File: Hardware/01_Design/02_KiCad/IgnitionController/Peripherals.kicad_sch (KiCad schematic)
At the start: 0 parts

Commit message: Peripherals Update
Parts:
- added C37, C38: 2.2uF, Capacitor_SMD:C_0805_2012Metric_Pad1.18x1.45mm_HandSolder, symbol Device:C
- added C39, C41: 1u, symbol Device:C_Small
- added C40, C42: 0.1u, symbol Device:C_Small
- added D19, D20, D21, D22: RED, symbol Device:LED
- added Q7: SS8050, Package_TO_SOT_SMD:TSOT-23_HandSoldering, symbol Transistor_BJT:SS8050
- added R40, R41: 10K, symbol Device:R_Small
- added R45: 43k, Resistor_SMD:R_0805_2012Metric_Pad1.20x1.40mm_HandSolder, symbol Device:R
- added R46, R47, R52, R53: 10K, Resistor_SMD:R_0805_2012Metric_Pad1.20x1.40mm_HandSolder, symbol Device:R
- added R48, R49: 360R, Resistor_SMD:R_0805_2012Metric_Pad1.20x1.40mm_HandSolder, symbol Device:R
- added R50, R51, R60, R65: 2K, symbol Device:R_Small
- added R59, R62, R63, R64: 100R, Resistor_SMD:R_0805_2012Metric_Pad1.20x1.40mm_HandSolder, symbol Device:R
- added U14: AT24CS01-SSHM, Package_SO:SOIC-8_3.9x4.9mm_P1.27mm, symbol Memory_EEPROM:AT24CS01-SSHM
- added U15: MCP2557FD-xSN, Package_SO:SOIC-8_3.9x4.9mm_P1.27mm, symbol Interface_CAN_LIN:MCP2557FD-xSN
- added U19, U20: IXDN602, symbol Library_sym.pretty:IXDN602SIA
- added U23, U24: 4N35, Package_DIP:DIP-6_W7.62mm, symbol Isolator:4N35
- added U25: TXS0104EPW, Package_SO:TSSOP-14_4.4x5mm_P0.65mm, symbol Logic_LevelTranslator:TXS0104EPW
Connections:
- new net: U14.6 (SCL), U25.10 (B4)
- new net: U14.5 (SDA), U25.11 (B3)
- new net: U15.4 (RXD), U25.12 (B2)
- new net: U15.1 (TXD), U25.13 (B1)
- new net: Q7.2 (E), R46.1, U25.8 (OE)
- new net: C38.1, R49.2, U24.1
- new net: R64.2, U20.4 (INB)
- new net: R47.1, U15.8 (S)
- new net: D20.2 (A), R60.2
- new net: R41.2, U24.6
- new net: R62.2, U19.4 (INB)
- new net: Q7.1 (B), R45.1
- new net: R59.2, U19.2 (INA)
- new net: R63.2, U20.2 (INA)
- new net: D19.2 (A), R50.2
- new net: D21.2 (A), R65.2
- new net: D22.2 (A), R51.2
- new net: C37.1, R48.2, U23.1
- new net: R40.2, U23.6
- new net CAN_RXD: U25.3 (A2)
- new net CAN_TXD: U25.2 (A1)
- new net Cylinder1Out_Pin: R59.1
- new net Cylinder2Out_Pin: R62.1
- new net Cylinder3Out_Pin: R63.1
- new net Cylinder4Out_Pin: R64.1
- new net GND: C37.2, C38.2, C39.2, C40.2, C41.2, C42.2, D19.1 (K), D20.1 (K), D21.1 (K), D22.1 (K), R40.1, R41.1, R46.2, R47.2, R52.2, R53.2, U14.1 (A0), U14.2 (A1), U14.3 (A2), U14.4 (GND), U14.7 (WP), U15.2 (VSS), U19.3 (GND), U20.3 (GND), U23.2, U24.2, U25.7 (GND)
- new net I2C_SCL: U25.5 (A4)
- new net I2C_SDA: U25.4 (A3)
- new net IGN_COIL_DRV_1: R50.1, U19.7 (OUTA)
- new net IGN_COIL_DRV_2: R60.1, U19.5 (OUTB)
- new net IGN_COIL_DRV_3: R51.1, U20.7 (OUTA)
- new net IGN_COIL_DRV_4: R65.1, U20.5 (OUTB)
- new net KL30_OUT: C39.1, C40.1, C41.1, C42.1, U19.6 (VCC), U20.6 (VCC)
- new net OE_PIN2: R45.2
- new net SENSOR_1_SIGNAL: R48.1
- new net SENSOR_2_SIGNAL: R49.1
- new net Signal1_Pin: R52.1, U23.4
- new net Signal2_Pin: R53.1, U24.4
- new net VMCU_OUT: Q7.3 (C), U23.5, U24.5, U25.1 (V_{CCA})
- new net VSEN_OUT: U14.8 (VCC), U15.3 (VDD), U25.14 (V_{CCB})
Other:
- note added: "Crank Input Optocouplers"
- note added: "Ignition Output Driver"

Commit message: Updates to HW Layout
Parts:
- added C43, C48, C49: 1u, Capacitor_SMD:C_0805_2012Metric_Pad1.18x1.45mm_HandSolder, symbol Device:C_Small
- added C44, C50, C51: 0.1u, Capacitor_SMD:C_0805_2012Metric_Pad1.18x1.45mm_HandSolder, symbol Device:C_Small
- added C45, C46: 100n, Capacitor_SMD:C_0805_2012Metric_Pad1.18x1.45mm_HandSolder, symbol Device:C
- added C47: 0.1u, Capacitor_SMD:C_0805_2012Metric_Pad1.18x1.45mm_HandSolder, symbol Device:C
- added D27, D28, D29, D30: RED, LED_SMD:LED_1206_3216Metric_Pad1.42x1.75mm_HandSolder, symbol Device:LED
- added R58: 120R, Resistor_SMD:R_0805_2012Metric_Pad1.20x1.40mm_HandSolder, symbol Device:R
- added R70, R74: 7K, Resistor_SMD:R_0805_2012Metric_Pad1.20x1.40mm_HandSolder, symbol Device:R
- added R71, R75, R76: 10K, Resistor_SMD:R_0805_2012Metric_Pad1.20x1.40mm_HandSolder, symbol Device:R
- added R72, R73: 8.2K, Resistor_SMD:R_0805_2012Metric_Pad1.20x1.40mm_HandSolder, symbol Device:R
- added R77, R78, R79, R80: 100R, Resistor_SMD:R_0805_2012Metric_Pad1.20x1.40mm_HandSolder, symbol Device:R
- added R81, R82, R83, R84: 2K, Resistor_SMD:R_0805_2012Metric_Pad1.20x1.40mm_HandSolder, symbol Device:R_Small
- added U13: TLV2372, Package_SO:SOIC-8_5.3x6.2mm_P1.27mm, symbol Amplifier_Operational:TLV2372
- added U16: MAX232, Package_SO:SOIC-16_3.9x9.9mm_P1.27mm, symbol Interface_UART:MAX232
- added U21, U22: IXDN602, Package_SO:SO-8_3.9x4.9mm_P1.27mm, symbol Library_sym.pretty:IXDN602SIA
- C39, C40, C41, C42: footprint (none) -> Capacitor_SMD:C_0805_2012Metric_Pad1.18x1.45mm_HandSolder
- D19, D20, D21, D22: footprint (none) -> LED_SMD:LED_1206_3216Metric_Pad1.42x1.75mm_HandSolder
- R40, R41, R50, R51, R60, R65: footprint (none) -> Resistor_SMD:R_0805_2012Metric_Pad1.20x1.40mm_HandSolder
- U19, U20: footprint (none) -> Package_SO:SO-8_3.9x4.9mm_P1.27mm
- U23, U24: footprint Package_DIP:DIP-6_W7.62mm -> 4N35S:4N35S
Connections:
- net GND: now also C43.2, C44.2, C45.2, C46.2, C47.2, C48.2, C49.2, C50.2, C51.2, D27.1 (K), D28.1 (K), D29.1 (K), D30.1 (K), R71.2, R75.2, U13.4 (V-), U21.3 (GND), U22.3 (GND)
- net KL30_OUT: now also C48.1, C49.1, C50.1, C51.1, U21.6 (VCC), U22.6 (VCC)
- net VMCU_OUT: now also R76.1
- net VSEN_OUT: now also C43.1, C44.1
- net CAN-L: now reaches U15.6 (CANL)
- net CAN-L: now also R58.1
- net CAN-H: now reaches U15.7 (CANH)
- net CAN-H: now also R58.2
- new net: R74.2, R75.1, U13.5 (+)
- new net: R73.2, U13.6 (-), U13.7
- new net: R78.2, U21.4 (INB)
- new net: R72.2, U13.1, U13.2 (-)
- new net: R70.2, R71.1, U13.3 (+)
- new net: R77.2, U21.2 (INA)
- new net: D29.2 (A), R83.2
- new net: R79.2, U22.2 (INA)
- new net: R80.2, U22.4 (INB)
- new net: D27.2 (A), R81.2
- new net: D28.2 (A), R82.2
- new net: D30.2 (A), R84.2
- new net COOLANT_TEMP_ADC_SIGNAL: C47.1, R76.2
- new net Cylinder1FuelOut_Pin: R77.1
- new net Cylinder2FuelOut_Pin: R78.1
- new net Cylinder3FuelOut_Pin: R79.1
- new net Cylinder4FuelOut_Pin: R80.1
- new net FUEL_INJ_DRV_1: R83.1, U21.7 (OUTA)
- new net FUEL_INJ_DRV_2: R81.1, U21.5 (OUTB)
- new net FUEL_INJ_DRV_3: R84.1, U22.7 (OUTA)
- new net FUEL_INJ_DRV_4: R82.1, U22.5 (OUTB)
- new net MAP_SENSOR_ADC_SIGNAL: C45.1, R72.1
- new net MAP_SENSOR_SIGNAL: R70.1
- new net TPS_ADC_SIGNAL: C46.1, R73.1
- new net TPS_SIGNAL: R74.1
- new net VPMIC: U13.8 (V+)
- no-connect marks 0 -> 8
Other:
- note added: "Engine Sensors"
- note added: "Fuel Injector Driver"
- moved on the sheet: C37, C38, C39, C40, C41, C42, D19, D20, D21, D22, Q7, R40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

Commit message: Initial routing of Power supply
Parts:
- C37, C38, C39, C40, C41, C42, C43, C44, C45, C46, C47, C48, C49, C50, C51: footprint Capacitor_SMD:C_0805_2012Metric_Pad1.18x1.45mm_HandSolder -> Capacitor_SMD:C_0603_1608Metric_Pad1.08x0.95mm_HandSolder
- R40, R41, R45, R46, R47, R48, R49, R50, R51, R52, R53, R58, R59, R60, R62, R63, R64, R65, R70, R71, R72, R73, R74, R75, R76, R77, R78, R79, R80, R81, R82, R83, R84: footprint Resistor_SMD:R_0805_2012Metric_Pad1.20x1.40mm_HandSolder -> Resistor_SMD:R_0603_1608Metric_Pad0.98x0.95mm_HandSolder

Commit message: Routing PCB done
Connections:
- net FUEL_INJ_DRV_2: no longer R81.1, U21.5 (OUTB)
- net MAP_SENSOR_ADC_SIGNAL: now also R72.2; no longer R72.1
- net TPS_ADC_SIGNAL: now also R73.2; no longer R73.1
- net at U13.6 (-), U13.7: now also R73.1; no longer R73.2
- net at U13.1, U13.2 (-): now also R72.1; no longer R72.2
- net at R81.2: now also U21.5 (OUTB); no longer D27.2 (A)
- new net: D27.2 (A), R81.1
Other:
- moved on the sheet: R72, R73, R81
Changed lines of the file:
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@@
 	(wire
 		(pts
-			(xy 452.12 148.59) (xy 471.17 148.59)
+			(xy 452.12 148.59) (xy 433.07 148.59)
 		)
 		(stroke
@@
 	(symbol
 		(lib_id "Device:R_Small")
-		(at 424.18 154.94 270)
-		(mirror x)
+		(at 424.18 154.94 90)
 		(unit 1)
 		(exclude_from_sim no)
@@
 		(on_board yes)
 		(dnp no)
-		(fields_autoplaced yes)
 		(property "Reference" "R81"
 			(at 424.18 160.02 90)
@@
 	(symbol
 		(lib_id "Device:R")
-		(at 104.14 242.57 90)
+		(at 104.14 242.57 270)
+		(mirror x)
 		(unit 1)
 		(exclude_from_sim no)
@@
 		(on_board yes)
 		(dnp no)
-		(fields_autoplaced yes)
 		(property "Reference" "R72"
 			(at 104.14 236.22 90)
@@
 	(symbol
 		(lib_id "Device:R")
-		(at 104.14 265.43 90)
+		(at 104.14 265.43 270)
+		(mirror x)
 		(unit 1)
 		(exclude_from_sim no)
@@
 		(on_board yes)
 		(dnp no)
-		(fields_autoplaced yes)
 		(property "Reference" "R73"
 			(at 104.14 259.08 90)

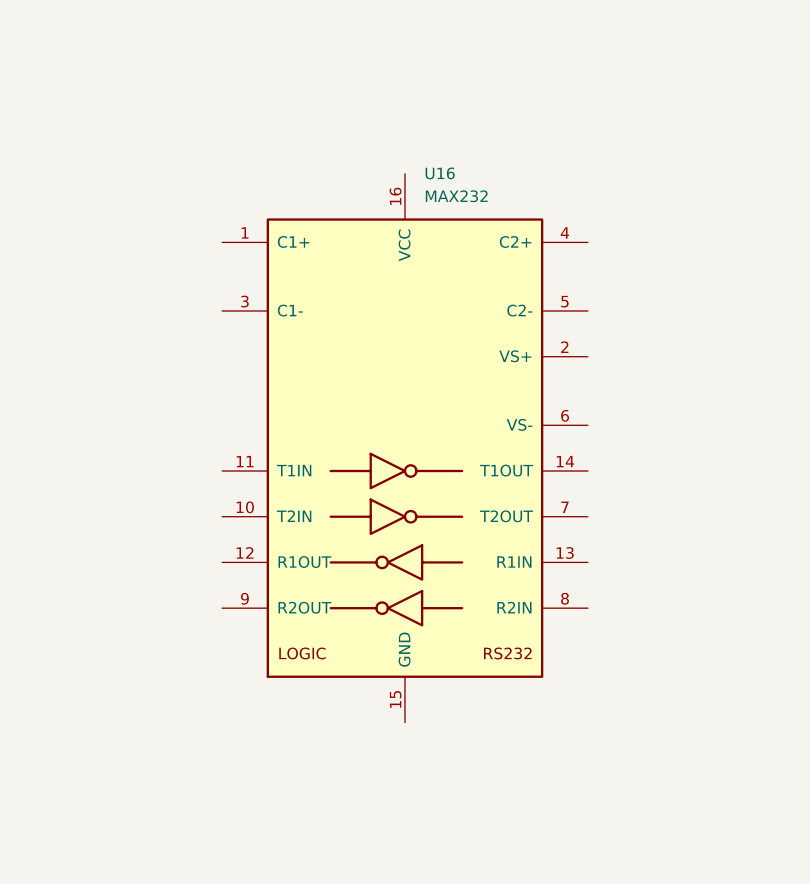
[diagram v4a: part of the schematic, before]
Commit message: Updated Solder Mask labels
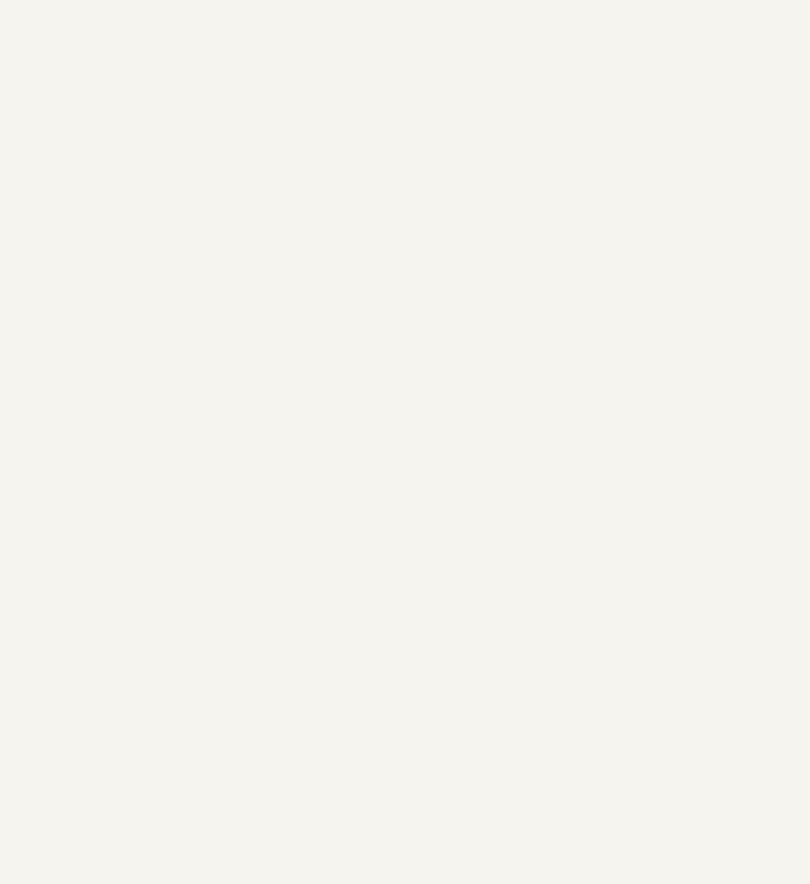
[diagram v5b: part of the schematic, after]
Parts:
- removed U16: MAX232, Package_SO:SOIC-16_3.9x9.9mm_P1.27mm, symbol Interface_UART:MAX232
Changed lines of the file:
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@@
-	)
-	(symbol
-		(lib_id "Interface_UART:MAX232")
-		(at 318.77 271.78 0)
-		(unit 1)
-		(exclude_from_sim no)
-		(in_bom yes)
-		(on_board yes)
-		(dnp no)
-		(fields_autoplaced yes)
-		(property "Reference" "U16"
-			(at 320.9133 241.3 0)
-			(effects
-				(font
-					(size 1.27 1.27)
-				)
-				(justify left)
-			)
-		)
-		(property "Value" "MAX232"
-			(at 320.9133 243.84 0)
-			(effects
-				(font
-					(size 1.27 1.27)
-				)
-				(justify left)
-			)
-		)
-		(property "Footprint" "Package_SO:SOIC-16_3.9x9.9mm_P1.27mm"
-			(at 320.04 298.45 0)
-			(effects
-				(font
-					(size 1.27 1.27)
-				)
-				(justify left)
-				(hide yes)
-			)
-		)
-		(property "Datasheet" "http://www.ti.com/lit/ds/symlink/max232.pdf"
-			(at 318.77 269.24 0)
-			(effects
-				(font
-					(size 1.27 1.27)
-				)
-				(hide yes)
-			)
-		)
-		(property "Description" "Dual RS232 driver/receiver, 5V supply, 120kb/s, 0C-70C"
-			(at 318.77 271.78 0)
-			(effects
-				(font
-					(size 1.27 1.27)
-				)
-				(hide yes)
-			)
-		)
-		(pin "16"
-		)
-		(pin "6"
-		)
-		(pin "13"
-		)
-		(pin "12"
-		)
-		(pin "15"
-		)
-		(pin "2"
-		)
-		(pin "8"
-		)
-		(pin "3"
-		)
-		(pin "1"
-		)
-		(pin "11"
-		)
-		(pin "10"
-		)
-		(pin "9"
-		)
-		(pin "4"
-		)
-		(pin "5"
-		)
-		(pin "14"
-		)
-		(pin "7"
-		)
-		(instances
-			(project ""
-				(path "/96744ec0-1e7f-4d75-9985-0095978419e2/b29964d9-34cb-4ba1-ac3a-194222ed2ea1"
-					(reference "U16")
-					(unit 1)
-				)
-			)
-		)
 	)
 	(symbol
